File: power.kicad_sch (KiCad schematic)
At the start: 60 parts, among them J4 Conn_01x02 DNI, J5 Conn_01x02 DNI, J6 Conn_01x02 DNI, Q29 AO3401, Q30 Q_NPN_BEC, T1 ACM7060(SMD Common Mode Choke), U14 NJM2845DL1-3.3, U19 TPS54428DDA, U2 TPS54202

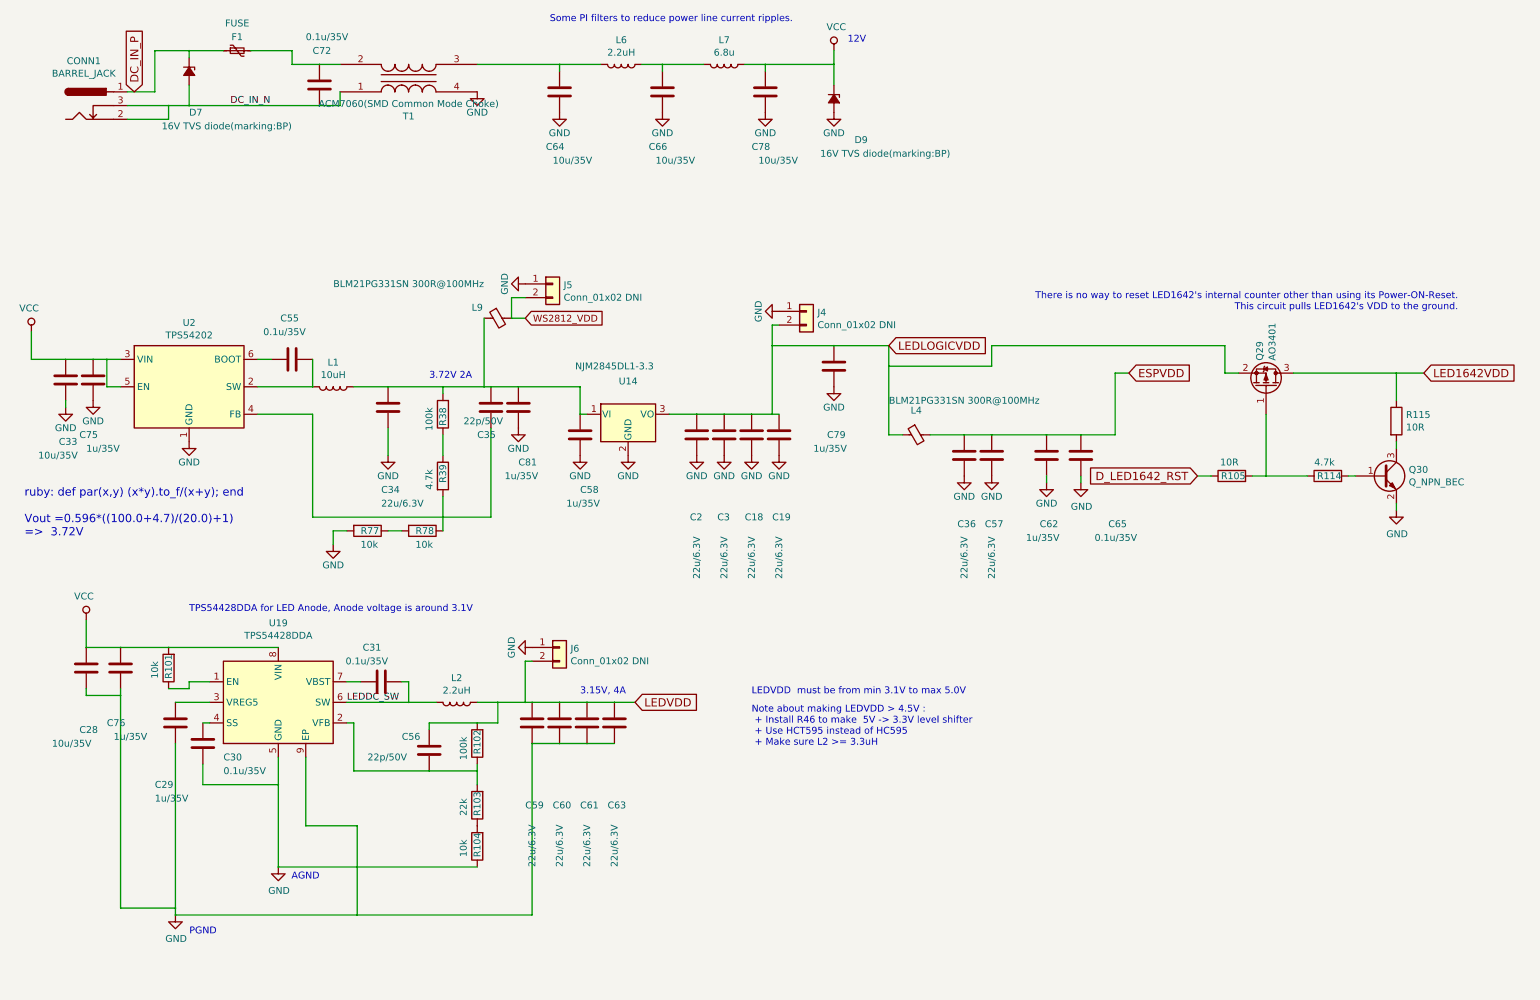
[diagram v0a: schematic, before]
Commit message: Experimental modification for audible noise redution at DC-DC converters
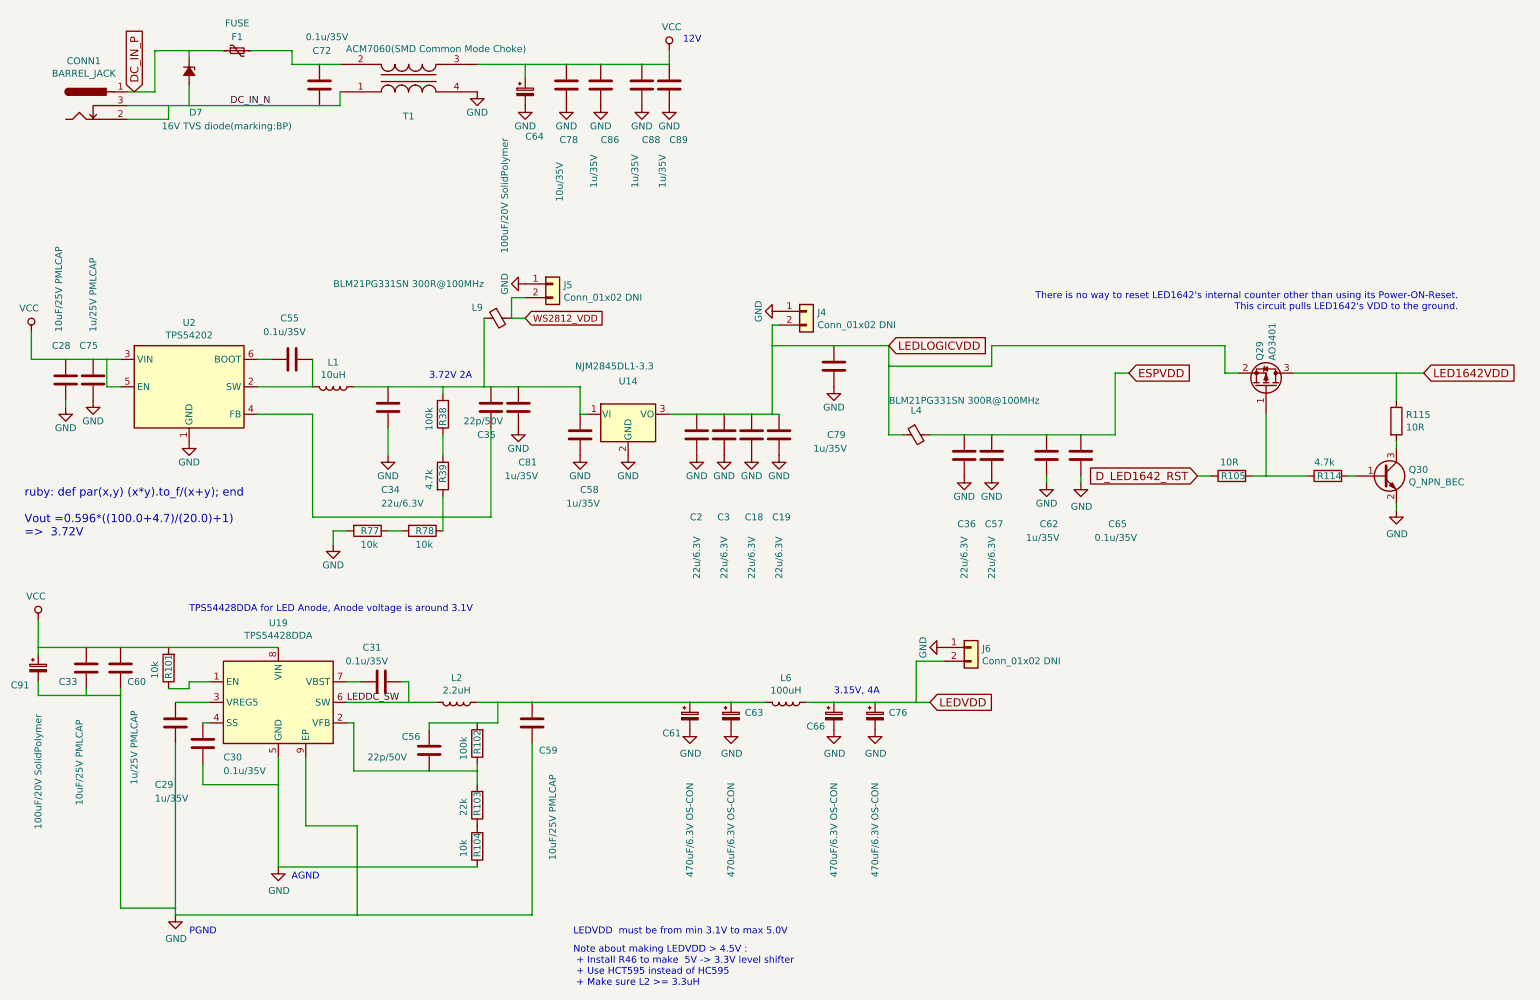
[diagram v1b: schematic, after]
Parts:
- removed C61, C63: 22u/6.3V, Capacitor_SMD:C_0603_1608Metric_Pad1.05x0.95mm_HandSolder, symbol dotmatrix_64x48-rescue:C-device
- removed C64, C66: 10u/35V, Capacitor_SMD:C_0603_1608Metric_Pad1.05x0.95mm_HandSolder, symbol dotmatrix_64x48-rescue:C-device
- removed C76: 1u/35V, Capacitor_SMD:C_0603_1608Metric_Pad1.05x0.95mm_HandSolder, symbol dotmatrix_64x48-rescue:C-device
- removed D9: 16V TVS diode(marking:BP), Diode_SMD:D_SMA_Handsoldering, symbol dotmatrix_64x48-rescue:D_Zener_Small_ALT-device
- removed L7: 6.8u, components:Choke_SMD_10.4x10.4_H4.8_HandSoldering, symbol dotmatrix_64x48-rescue:L-device
- added C61, C63, C66, C76: 470uF/6.3V OS-CON, Capacitor_SMD:CP_Elec_6.3x9.9, symbol device:CP_Small
- added C64, C91: 100uF/20V SolidPolymer, Capacitor_SMD:CP_Elec_10x10, symbol device:CP_Small
- added C86, C88, C89: 1u/35V, Capacitor_SMD:C_0603_1608Metric_Pad1.08x0.95mm_HandSolder, symbol dotmatrix_64x48-rescue:C-device
- C28, C33: value 10u/35V -> 10uF/25V PMLCAP; footprint Capacitor_SMD:C_0603_1608Metric_Pad1.05x0.95mm_HandSolder -> components:C_0603_1608Metric_to_2220_5650Metric_Multi_HandSolder
- C59: value 22u/6.3V -> 10uF/25V PMLCAP; footprint Capacitor_SMD:C_0603_1608Metric_Pad1.05x0.95mm_HandSolder -> components:C_0603_1608Metric_to_2220_5650Metric_Multi_HandSolder
- C60: value 22u/6.3V -> 1u/25V PMLCAP; footprint Capacitor_SMD:C_0603_1608Metric_Pad1.05x0.95mm_HandSolder -> components:C_0603_1608Metric_to_1206_3216Metric_Multi_HandSolder
- C75: value 1u/35V -> 1u/25V PMLCAP; footprint Capacitor_SMD:C_0603_1608Metric_Pad1.05x0.95mm_HandSolder -> components:C_0603_1608Metric_to_1206_3216Metric_Multi_HandSolder
- C78: footprint Capacitor_SMD:C_0603_1608Metric_Pad1.05x0.95mm_HandSolder -> Capacitor_SMD:C_0603_1608Metric_Pad1.08x0.95mm_HandSolder
- L6: value 2.2uH -> 100uH; footprint components:Choke_SMD_10.4x10.4_H4.8_HandSoldering -> components:Inductor-SMD-18x17-Handsoldering
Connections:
- net GND: now also C61.2, C63.2, C64.2, C66.2, C76.2, C86.2, C88.2, C89.2, C91.2
- net LEDVDD: now also L6.1, C66.1, C76.1; no longer C56.1, C59.1, C60.1, L2.1, R102.2
- net VCC: now also C60.1, T1.3, C64.1, C86.1, C88.1, C89.1, C91.1
- net at L6.2: now also C56.1, C59.1, L2.1, R102.2, C61.1, C63.1; no longer T1.3
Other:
- note removed: "Some PI filters to reduce power line current ripples."
- moved on the sheet: J6

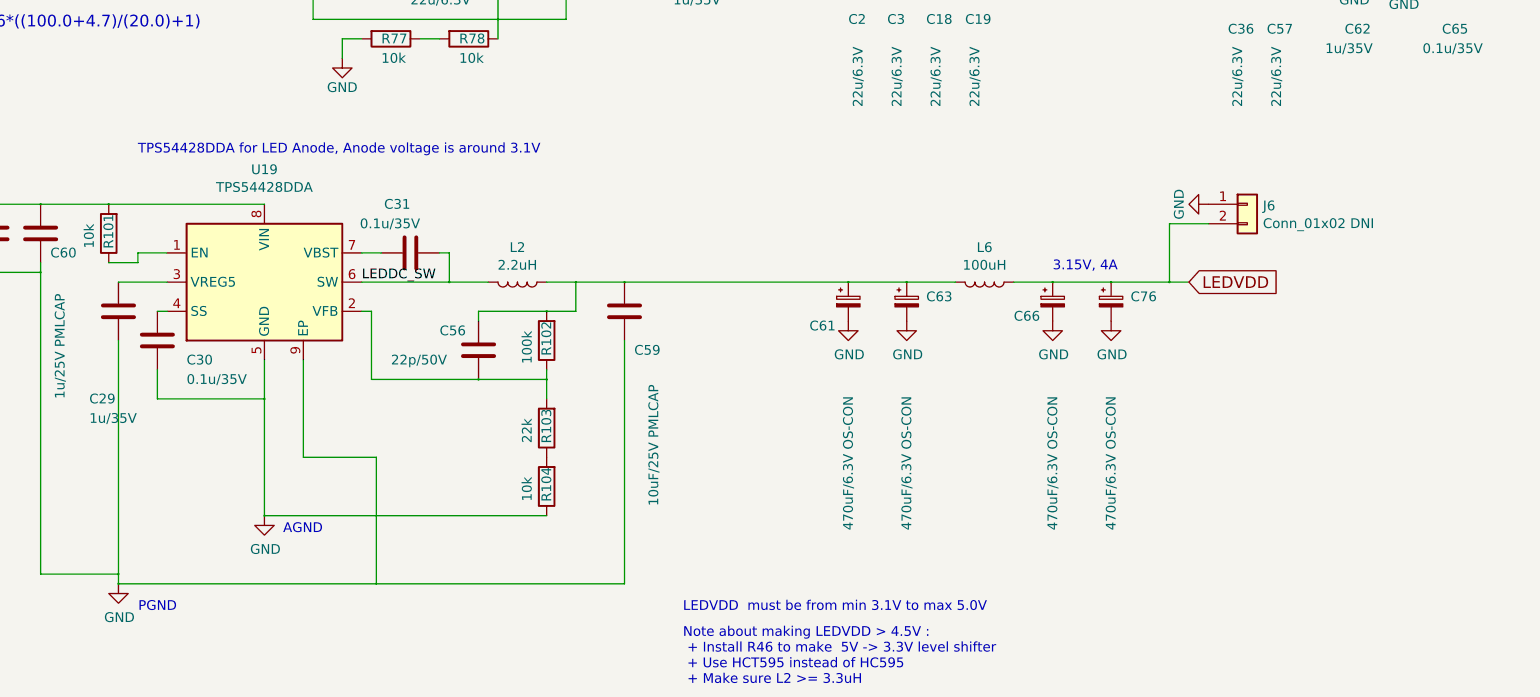
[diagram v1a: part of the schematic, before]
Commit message: Improved audible noize reduction; DRC clear
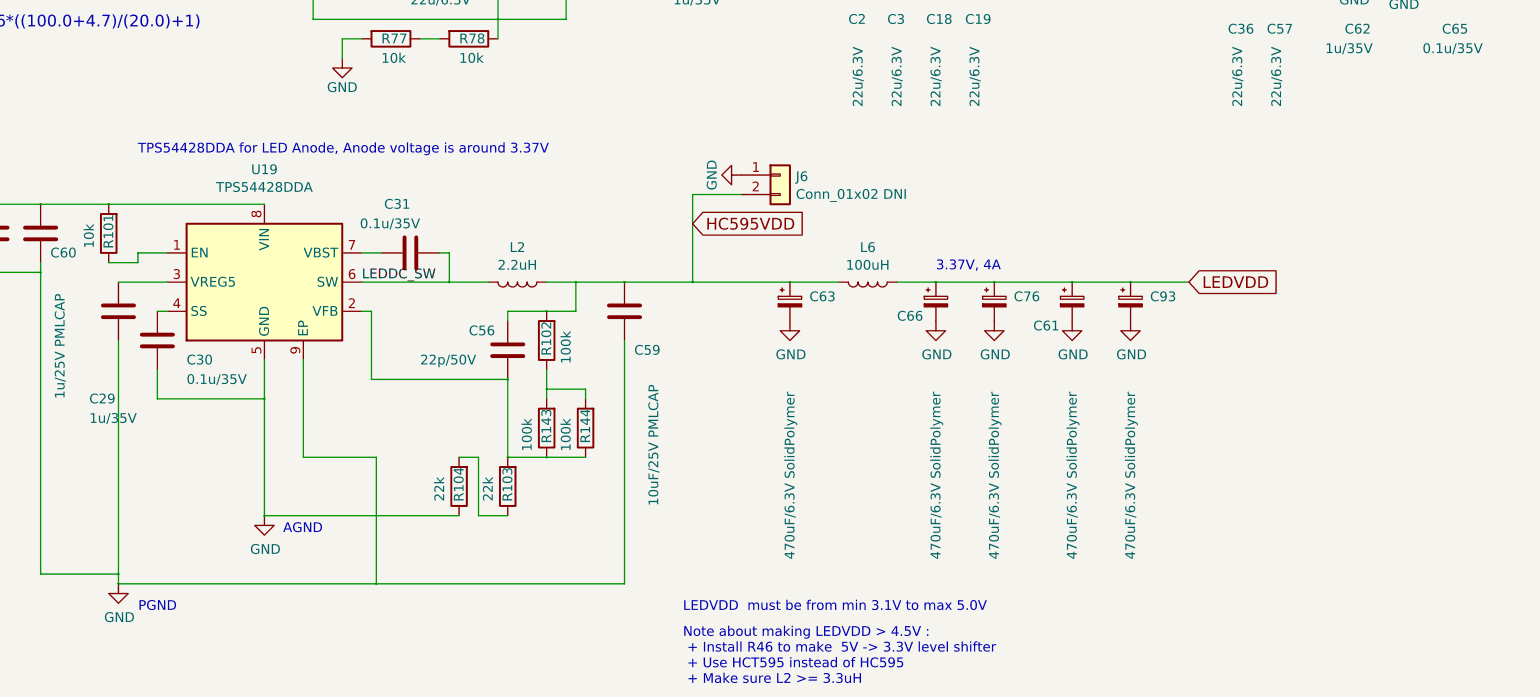
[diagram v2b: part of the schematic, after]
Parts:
- added C93: 470uF/6.3V SolidPolymer, Capacitor_THT:CP_Radial_D6.3mm_P2.50mm, symbol device:CP_Small
- added R143, R144: 100k, Resistor_SMD:R_0603_1608Metric_Pad0.98x0.95mm_HandSolder, symbol dotmatrix_64x48-rescue:R-device
- C61, C63, C66, C76: value 470uF/6.3V OS-CON -> 470uF/6.3V SolidPolymer; footprint Capacitor_SMD:CP_Elec_6.3x9.9 -> Capacitor_THT:CP_Radial_D6.3mm_P2.50mm
- R102, R103: footprint Resistor_SMD:R_0603_1608Metric_Pad1.05x0.95mm_HandSolder -> Resistor_SMD:R_0603_1608Metric_Pad0.98x0.95mm_HandSolder
- R104: value 10k -> 22k; footprint Resistor_SMD:R_0603_1608Metric_Pad1.05x0.95mm_HandSolder -> Resistor_SMD:R_0603_1608Metric_Pad0.98x0.95mm_HandSolder
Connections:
- net GND: now also C93.2
- net LEDVDD: now also C61.1, C93.1; no longer J6.2 (Pin_2)
- net at C56.2, R103.2, U19.2 (VFB): now also R143.1, R144.1; no longer R102.1
- net HC595VDD: now reaches C56.1, C59.1, C63.1, L2.1, L6.2, R102.2
- net HC595VDD: now also J6.2 (Pin_2); no longer C61.1
- new net: R102.1, R143.2, R144.2
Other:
- note added: "3.37V, 4A"
- note added: "TPS54428DDA for LED Anode, Anode voltage is around 3.37V"
- note removed: "3.15V, 4A"
- note removed: "TPS54428DDA for LED Anode, Anode voltage is around 3.1V"
- moved on the sheet: C56, C63, C66, C76, J6, L6, R103, R104

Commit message: Removed PML caps; I concluded they do not help audible noise reduction; DRC clear
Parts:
- C28, C33: value 10uF/25V PMLCAP -> 10u/35V; footprint components:C_0603_1608Metric_to_2220_5650Metric_Multi_HandSolder -> Capacitor_SMD:C_0603_1608Metric_Pad1.08x0.95mm_HandSolder
- C59: value 10uF/25V PMLCAP -> 1u/35V; footprint components:C_0603_1608Metric_to_2220_5650Metric_Multi_HandSolder -> Capacitor_SMD:C_0603_1608Metric_Pad1.08x0.95mm_HandSolder
- C60: value 1u/25V PMLCAP -> 1u/35V; footprint components:C_0603_1608Metric_to_1206_3216Metric_Multi_HandSolder -> Capacitor_SMD:C_0603_1608Metric_Pad1.08x0.95mm_HandSolder
- C75: value 1u/25V PMLCAP -> 10u/35V; footprint components:C_0603_1608Metric_to_1206_3216Metric_Multi_HandSolder -> Capacitor_SMD:C_0603_1608Metric_Pad1.08x0.95mm_HandSolder
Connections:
- net HC595VDD: now also C75.1; no longer C59.1
- net VCC: now also C59.1; no longer C75.1
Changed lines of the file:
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@@
   (symbol (lib_id "dotmatrix_64x48-rescue:C-device") (at 21.59 85.09 0) (unit 1)
     (in_bom yes) (on_board yes)
-    (property "Reference" "C28" (id 0) (at 19.05 78.74 0)
-      (effects (font (size 1.27 1.27)) (justify left))
-    )
-    (property "Value" "10uF/25V PMLCAP" (id 1) (at 20.32 76.2 90)
-      (effects (font (size 1.27 1.27)) (justify left))
-    )
-    (property "Footprint" "components:C_0603_1608Metric_to_2220_5650Metric_Multi_HandSolder" (id 2) (at 24.511 87.4014 0)
+    (property "Reference" "C28" (id 0) (at 17.78 97.79 0)
+      (effects (font (size 1.27 1.27)) (justify left))
+    )
+    (property "Value" "10u/35V" (id 1) (at 12.7 100.33 0)
+      (effects (font (size 1.27 1.27)) (justify left))
+    )
+    (property "Footprint" "Capacitor_SMD:C_0603_1608Metric_Pad1.08x0.95mm_HandSolder" (id 2) (at 24.511 87.4014 0)
       (effects (font (size 1.27 1.27)) (justify left) hide)
     )
@@
   (symbol (lib_id "dotmatrix_64x48-rescue:C-device") (at 25.4 138.43 0) (unit 1)
     (in_bom yes) (on_board yes)
-    (property "Reference" "C33" (id 0) (at 20.32 140.97 0)
-      (effects (font (size 1.27 1.27)) (justify left))
-    )
-    (property "Value" "10uF/25V PMLCAP" (id 1) (at 24.13 163.83 90)
-      (effects (font (size 1.27 1.27)) (justify left))
-    )
-    (property "Footprint" "components:C_0603_1608Metric_to_2220_5650Metric_Multi_HandSolder" (id 2) (at 28.321 140.7414 0)
+    (property "Reference" "C33" (id 0) (at 22.86 146.05 0)
+      (effects (font (size 1.27 1.27)) (justify left))
+    )
+    (property "Value" "10u/35V" (id 1) (at 19.05 149.86 0)
+      (effects (font (size 1.27 1.27)) (justify left))
+    )
+    (property "Footprint" "Capacitor_SMD:C_0603_1608Metric_Pad1.08x0.95mm_HandSolder" (id 2) (at 28.321 140.7414 0)
       (effects (font (size 1.27 1.27)) (justify left) hide)
     )
@@
   (symbol (lib_id "dotmatrix_64x48-rescue:C-device") (at 26.67 85.09 0) (unit 1)
     (in_bom yes) (on_board yes)
-    (property "Reference" "C75" (id 0) (at 24.13 78.74 0)
-      (effects (font (size 1.27 1.27)) (justify left))
-    )
-    (property "Value" "1u/25V PMLCAP" (id 1) (at 26.67 76.2 90)
-      (effects (font (size 1.27 1.27)) (justify left))
-    )
-    (property "Footprint" "components:C_0603_1608Metric_to_1206_3216Metric_Multi_HandSolder" (id 2) (at 29.591 87.4014 0)
+    (property "Reference" "C59" (id 0) (at 25.4 97.79 0)
+      (effects (font (size 1.27 1.27)) (justify left))
+    )
+    (property "Value" "1u/35V" (id 1) (at 22.86 100.33 0)
+      (effects (font (size 1.27 1.27)) (justify left))
+    )
+    (property "Footprint" "Capacitor_SMD:C_0603_1608Metric_Pad1.08x0.95mm_HandSolder" (id 2) (at 29.591 87.4014 0)
       (effects (font (size 1.27 1.27)) (justify left) hide)
     )
@@
   (symbol (lib_id "dotmatrix_64x48-rescue:C-device") (at 31.75 138.43 0) (unit 1)
     (in_bom yes) (on_board yes)
-    (property "Reference" "C60" (id 0) (at 33.02 140.97 0)
-      (effects (font (size 1.27 1.27)) (justify left))
-    )
-    (property "Value" "1u/25V PMLCAP" (id 1) (at 34.29 160.02 90)
-      (effects (font (size 1.27 1.27)) (justify left))
-    )
-    (property "Footprint" "components:C_0603_1608Metric_to_1206_3216Metric_Multi_HandSolder" (id 2) (at 34.671 140.7414 0)
+    (property "Reference" "C60" (id 0) (at 31.75 146.05 0)
+      (effects (font (size 1.27 1.27)) (justify left))
+    )
+    (property "Value" "1u/35V" (id 1) (at 29.21 149.86 0)
+      (effects (font (size 1.27 1.27)) (justify left))
+    )
+    (property "Footprint" "Capacitor_SMD:C_0603_1608Metric_Pad1.08x0.95mm_HandSolder" (id 2) (at 34.671 140.7414 0)
       (effects (font (size 1.27 1.27)) (justify left) hide)
     )
@@
   (symbol (lib_id "dotmatrix_64x48-rescue:C-device") (at 107.95 148.59 0) (unit 1)
     (in_bom yes) (on_board yes)
-    (property "Reference" "C59" (id 0) (at 109.22 153.67 0)
-      (effects (font (size 1.27 1.27)) (justify left))
-    )
-    (property "Value" "10uF/25V PMLCAP" (id 1) (at 111.76 173.99 90)
-      (effects (font (size 1.27 1.27)) (justify left))
-    )
-    (property "Footprint" "components:C_0603_1608Metric_to_2220_5650Metric_Multi_HandSolder" (id 2) (at 110.871 150.9014 0)
-      (effects (font (size 1.27 1.27)) (justify left) hide)
-    )
+    (property "Reference" "C75" (id 0) (at 109.22 152.4 0)
+      (effects (font (size 1.27 1.27)) (justify left))
+    )
+    (property "Value" "10u/35V" (id 1) (at 109.22 154.94 0)
+      (effects (font (size 1.27 1.27)) (justify left))
+    )
+    (property "Footprint" "Capacitor_SMD:C_0603_1608Metric_Pad1.08x0.95mm_HandSolder" (id 2) (at 110.871 150.9014 0)
+      (effects (font (size 1.27 1.27)) (justify left) hide)
+    )

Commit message: Reverted L2 value to 6.8uH (Sorry I have bought too many 6.8uH'sgit statusgit status)
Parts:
- L2: value 2.2uH -> 2.2uH to 6.8uH
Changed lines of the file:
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@@
     (in_bom yes) (on_board yes)
     (property "Reference" "L2" (id 0) (at 93.98 140.2588 90))
-    (property "Value" "2.2uH" (id 1) (at 93.98 142.57 90))
+    (property "Value" "2.2uH to 6.8uH" (id 1) (at 93.98 142.57 90))
     (property "Footprint" "components:Choke_SMD_10.4x10.4_H4.8_HandSoldering" (id 2) (at 93.98 144.78 0)
       (effects (font (size 1.27 1.27)) hide)
